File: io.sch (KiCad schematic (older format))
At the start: 12 parts, among them X1 CON-JST_SM04B-SRSS-TB, X2 CON-JST_SM04B-SRSS-TB, X3 CON-JST_SM04B-SRSS-TB, X4 CON-JST_SM04B-SRSS-TB, X5 CON-JST_SM04B-SRSS-TB, X6 CON-JST_SM04B-SRSS-TB, X7 CON-JST_SM04B-SRSS-TB, X8 CON-JST_SM04B-SRSS-TB

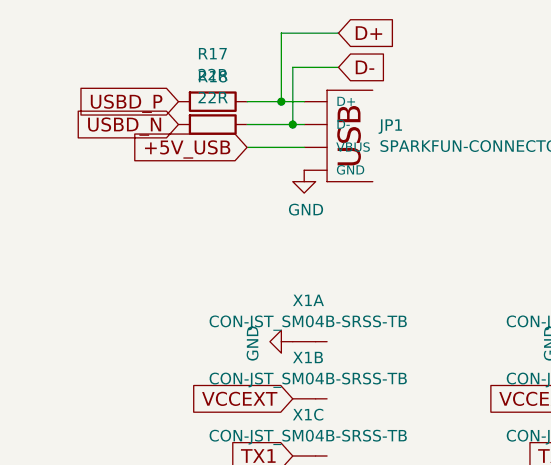
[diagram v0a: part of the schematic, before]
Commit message: added i2c pullups, IMU int and USB sense
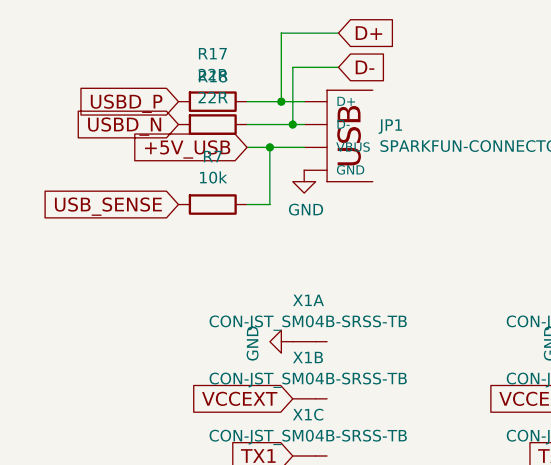
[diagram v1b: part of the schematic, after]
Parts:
- added R7: 10k, Resistors_SMD:R_0402, symbol R
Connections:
- net +5V_USB: now also R7.1
- new net USB_SENSE: R7.2
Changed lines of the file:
@@
 LIBS:contrib
 LIBS:valves
-LIBS:minimal
 LIBS:alis_parts
 LIBS:stm32f4_lqfp64_mpu6050-cache
@@
 Text GLabel 3500 4300 0    60   Input ~ 0
 VCC
-Wire Wire Line
-	6200 3100 6350 3100
 Text GLabel 7700 4800 0    60   Input ~ 0
 PWM4
@@
 $EndComp
 $Comp
-L GND #PWR6
+L GND #PWR01
 U 1 1 5699735E
 P 7650 3350
-F 0 "#PWR6" H 7650 3100 50  0001 C CNN
+F 0 "#PWR01" H 7650 3100 50  0001 C CNN
 F 1 "GND" H 7658 3176 50  0000 C CNN
 F 2 "" H 7650 3350 50  0000 C CNN
@@
 TX5
 $Comp
-L GND #PWR4
+L GND #PWR02
 U 1 1 56997382
 P 4800 2850
-F 0 "#PWR4" H 4800 2600 50  0001 C CNN
+F 0 "#PWR02" H 4800 2600 50  0001 C CNN
 F 1 "GND" H 4808 2676 50  0000 C CNN
 F 2 "" H 4800 2850 50  0000 C CNN
@@
 TX4
 $Comp
-L GND #PWR8
+L GND #PWR03
 U 1 1 569973A7
 P 6300 4050
-F 0 "#PWR8" H 6300 3800 50  0001 C CNN
+F 0 "#PWR03" H 6300 3800 50  0001 C CNN
 F 1 "GND" H 6308 3876 50  0000 C CNN
 F 2 "" H 6300 4050 50  0000 C CNN
@@
 TX3
 $Comp
-L GND #PWR7
+L GND #PWR04
 U 1 1 569973CC
 P 3500 4050
-F 0 "#PWR7" H 3500 3800 50  0001 C CNN
+F 0 "#PWR04" H 3500 3800 50  0001 C CNN
 F 1 "GND" H 3508 3876 50  0000 C CNN
 F 2 "" H 3500 4050 50  0000 C CNN
@@
 $EndComp
 $Comp
-L GND #PWR5
+L GND #PWR05
 U 1 1 569973EE
 P 6350 2850
-F 0 "#PWR5" H 6350 2600 50  0001 C CNN
+F 0 "#PWR05" H 6350 2600 50  0001 C CNN
 F 1 "GND" H 6358 2676 50  0000 C CNN
 F 2 "" H 6350 2850 50  0000 C CNN
@@
 TX1
 $Comp
-L GND #PWR3
+L GND #PWR06
 U 1 1 56997413
 P 3500 2850
-F 0 "#PWR3" H 3500 2600 50  0001 C CNN
+F 0 "#PWR06" H 3500 2600 50  0001 C CNN
 F 1 "GND" H 3508 2676 50  0000 C CNN
 F 2 "" H 3500 2850 50  0000 C CNN
@@
 $EndComp
 $Comp
-L GND #PWR2
+L GND #PWR07
 U 1 1 569B0BD9
 P 3550 2100
-F 0 "#PWR2" H 3550 1850 50  0001 C CNN
+F 0 "#PWR07" H 3550 1850 50  0001 C CNN
 F 1 "GND" H 3558 1926 50  0000 C CNN
 F 2 "" H 3550 2100 50  0000 C CNN
@@
 Text GLabel 3700 1650 2    60   Input ~ 0
 D-
-Wire Wire Line
-	3300 1800 3550 1800
-Wire Wire Line
-	3300 1900 3550 1900
-Wire Wire Line
-	3300 2000 3550 2000
-Wire Wire Line
-	3500 1650 3700 1650
-Wire Wire Line
-	3700 1500 3450 1500
-Wire Wire Line
-	3450 1500 3450 1800
-Connection ~ 3450 1800
-Wire Wire Line
-	3500 1650 3500 1900
-Connection ~ 3500 1900
 $Comp
 L R R4
@@
 Text GLabel 7300 1950 2    60   Input ~ 0
 VCCEXT
+$Comp
+L R R7
+U 1 1 570559BC
+P 3150 2250
+F 0 "R7" V 2942 2250 50  0000 C CNN
+F 1 "10k" V 3034 2250 50  0000 C CNN
+F 2 "Resistors_SMD:R_0402" V 3080 2250 50  0001 C CNN
+F 3 "" H 3150 2250 50  0000 C CNN
+	1    3150 2250
+	0    1    1    0
+$EndComp
+Wire Wire Line
+	6200 3100 6350 3100
+Wire Wire Line
+	3300 1800 3550 1800
+Wire Wire Line
+	3300 1900 3550 1900
+Wire Wire Line
+	3300 2000 3550 2000
+Wire Wire Line
+	3500 1650 3700 1650
+Wire Wire Line
+	3700 1500 3450 1500
+Wire Wire Line
+	3450 1500 3450 1800
+Connection ~ 3450 1800
+Wire Wire Line
+	3500 1650 3500 1900
+Connection ~ 3500 1900
+Wire Wire Line
+	3300 2250 3400 2250
+Wire Wire Line
+	3400 2250 3400 2000
+Connection ~ 3400 2000
+Text GLabel 3000 2250 0    60   Input ~ 0
+USB_SENSE
 $EndSCHEMATC
